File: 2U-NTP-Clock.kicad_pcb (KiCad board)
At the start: 2 copper layers, 482.6 x 83.8 mm, 279 parts, among them J1 Barrel_Jack_Switch, J2 Conn_01x06_Socket, Q1 BSS138, Q10 BSS138, Q11 BSS138, Q12 BSS138, Q13 BSS138, Q14 BSS138, Q15 BSS138, Q16 BSS138, Q17 BSS138, Q18 BSS138, Q19 BSS138, Q2 BSS138, Q20 BSS138, Q21 BSS138, Q22 BSS138, Q23 BSS138, Q24 BSS138, Q25 BSS138, Q26 BSS138, Q27 BSS138, Q28 BSS138, Q29 BSS138, Q3 BSS138, Q30 BSS138, Q31 BSS138, Q32 BSS138, Q33 BSS138, Q34 BSS138, Q35 BSS138, Q36 BSS138, Q37 BSS138, Q38 BSS138, Q39 BSS138, Q4 BSS138, Q40 BSS138, Q41 BSS138, Q42 BSS138, Q43 BSS138, Q5 BSS138, Q6 BSS138, Q7 BSS138, Q8 BSS138, Q9 BSS138, SW1 SW_Push, SW2 SW_Push, SW3 SW_Push, SW4 SW_Push, SW5 SW_Push, SW6 SW_Slide_DPDT, U3 74HC595, U4 74HC595, U5 74HC595, U6 74HC595, U7 74HC595, U8 74HC595, U9 L7805

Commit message: 基板概形修正
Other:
- board size 482.6 x 83.8 mm -> 482.6 x 87.8 mm
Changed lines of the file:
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@@
 	)
 	(gr_arc
-		(start 546.099999 241.299998)
-		(mid 544.984076 243.994075)
-		(end 542.289999 245.109998)
+		(start 546.1 243.332)
+		(mid 544.984077 246.026078)
+		(end 542.29 247.142)
 		(stroke
 			(width 0.05)
@@
 	)
 	(gr_line
-		(start 67.31 161.289999)
-		(end 542.289999 161.29)
+		(start 114.935 166.116)
+		(end 114.935 173.609)
 		(stroke
 			(width 0.05)
@@
 	)
 	(gr_arc
-		(start 539.242 174.243999)
-		(mid 542.798 177.799999)
-		(end 539.242 181.355999)
+		(start 118.745 173.609)
+		(mid 118.521815 174.147815)
+		(end 117.983 174.371)
 		(stroke
 			(width 0.05)
@@
 	)
 	(gr_line
-		(start 73.66 232.155999)
-		(end 70.358 232.155999)
+		(start 67.310001 159.384999)
+		(end 542.29 159.385)
 		(stroke
 			(width 0.05)
@@
 	)
 	(gr_arc
-		(start 535.94 232.155999)
-		(mid 532.384 228.599999)
-		(end 535.94 225.043999)
+		(start 539.242 177.418999)
+		(mid 542.798001 180.975)
+		(end 539.242 184.530999)
 		(stroke
 			(width 0.05)
@@
 	)
 	(gr_line
-		(start 63.5 241.299999)
-		(end 63.5 165.099999)
+		(start 73.66 228.980999)
+		(end 70.358 228.980999)
 		(stroke
 			(width 0.05)
@@
 	)
 	(gr_arc
-		(start 73.66 225.043999)
-		(mid 77.216 228.599999)
-		(end 73.66 232.155999)
+		(start 535.94 228.980999)
+		(mid 532.384001 225.425)
+		(end 535.94 221.868999)
+		(stroke
+			(width 0.05)
+			(type default)
+		)
+		(layer "Edge.Cuts")
+	)
+	(gr_line
+		(start 63.500001 243.332001)
+		(end 63.500001 163.194999)
+		(stroke
+			(width 0.05)
+			(type default)
+		)
+		(layer "Edge.Cuts")
+	)
+	(gr_arc
+		(start 73.66 221.868999)
+		(mid 77.216001 225.425)
+		(end 73.66 228.980999)
+		(stroke
+			(width 0.05)
+			(type default)
+		)
+		(layer "Edge.Cuts")
+	)
+	(gr_arc
+		(start 539.242 221.868999)
+		(mid 542.798001 225.425)
+		(end 539.242 228.980999)
+		(stroke
+			(width 0.05)
+			(type default)
+		)
+		(layer "Edge.Cuts")
+	)
+	(gr_line
+		(start 539.242 228.980999)
+		(end 535.94 228.980999)
 		(stroke
 			(width 0.05)
@@
 	)
 	(gr_arc
-		(start 539.242 225.043999)
-		(mid 542.798 228.599999)
-		(end 539.242 232.155999)
+		(start 535.94 184.530999)
+		(mid 532.384001 180.975)
+		(end 535.94 177.418999)
 		(stroke
 			(width 0.05)
@@
 	)
 	(gr_line
-		(start 539.242 232.155999)
-		(end 535.94 232.155999)
+		(start 118.745 173.609)
+		(end 118.745 166.116)
 		(stroke
 			(width 0.05)
@@
 	)
 	(gr_arc
-		(start 535.94 181.355999)
-		(mid 532.384 177.799999)
-		(end 535.94 174.243999)
+		(start 67.310001 247.142001)
+		(mid 64.615925 246.026078)
+		(end 63.500001 243.332001)
+		(stroke
+			(width 0.05)
+			(type default)
+		)
+		(layer "Edge.Cuts")
+	)
+	(gr_line
+		(start 542.29 247.142)
+		(end 67.310001 247.142001)
 		(stroke
 			(width 0.05)
@@
 	)
 	(gr_arc
-		(start 67.31 245.109999)
-		(mid 64.615923 243.994076)
-		(end 63.5 241.299999)
+		(start 70.358 228.980999)
+		(mid 66.802001 225.425)
+		(end 70.358 221.868999)
 		(stroke
 			(width 0.05)
@@
 	)
 	(gr_line
-		(start 542.289999 245.109998)
-		(end 67.31 245.109999)
+		(start 546.1 163.322)
+		(end 546.1 243.332)
 		(stroke
 			(width 0.05)
@@
 	)
 	(gr_arc
-		(start 70.358 232.155999)
-		(mid 66.802 228.599999)
-		(end 70.358 225.043999)
+		(start 115.697 174.371)
+		(mid 115.158185 174.147815)
+		(end 114.935 173.609)
+		(stroke
+			(width 0.05)
+			(type default)
+		)
+		(layer "Edge.Cuts")
+	)
+	(gr_line
+		(start 115.697 174.371)
+		(end 117.983 174.371)
 		(stroke
 			(width 0.05)
@@
 	)
 	(gr_line
-		(start 546.099999 165.1)
-		(end 546.1 241.299999)
+		(start 539.242 184.530999)
+		(end 535.94 184.530999)
 		(stroke
 			(width 0.05)
@@
 	)
 	(gr_line
-		(start 539.242 181.355999)
-		(end 535.94 181.355999)
+		(start 73.66 184.530999)
+		(end 70.358 184.530999)
 		(stroke
 			(width 0.05)
@@
 	)
 	(gr_line
-		(start 73.66 181.355999)
-		(end 70.358 181.355999)
+		(start 115.697 165.354)
+		(end 117.983 165.354)
 		(stroke
 			(width 0.05)
@@
 	)
 	(gr_line
-		(start 70.358 225.043999)
-		(end 73.66 225.043999)
+		(start 70.358 221.868999)
+		(end 73.66 221.868999)
+		(stroke
+			(width 0.05)
+			(type default)
+		)
+		(layer "Edge.Cuts")
+	)
+	(gr_arc
+		(start 63.500001 163.194999)
+		(mid 64.615925 160.500923)
+		(end 67.310001 159.384999)
+		(stroke
+			(width 0.05)
+			(type default)
+		)
+		(layer "Edge.Cuts")
+	)
+	(gr_arc
+		(start 117.983 165.354)
+		(mid 118.521815 165.577185)
+		(end 118.745 166.116)
 		(stroke
 			(width 0.05)
@@
 	)
 	(gr_arc
-		(start 63.5 165.099999)
-		(mid 64.615923 162.405922)
-		(end 67.31 161.289999)
+		(start 542.29 159.385)
+		(mid 544.984077 160.500923)
+		(end 546.1 163.195)
 		(stroke
 			(width 0.05)
@@
 	)
 	(gr_arc
-		(start 542.289999 161.29)
-		(mid 544.984076 162.405923)
-		(end 546.099999 165.1)
+		(start 114.935 166.116)
+		(mid 115.158185 165.577185)
+		(end 115.697 165.354)
 		(stroke
 			(width 0.05)
@@
 	)
 	(gr_arc
-		(start 73.66 174.243999)
-		(mid 77.216 177.799999)
-		(end 73.66 181.355999)
+		(start 73.66 177.418999)
+		(mid 77.216001 180.975)
+		(end 73.66 184.530999)
 		(stroke
 			(width 0.05)
@@
 	)
 	(gr_line
-		(start 535.94 225.043999)
-		(end 539.242 225.043999)
+		(start 535.94 221.868999)
+		(end 539.242 221.868999)
 		(stroke
 			(width 0.05)
@@
 	)
 	(gr_line
-		(start 70.358 174.243999)
-		(end 73.66 174.243999)
+		(start 70.358 177.418999)
+		(end 73.66 177.418999)
 		(stroke
 			(width 0.05)
@@
 	)
 	(gr_arc
-		(start 70.358 181.355999)
-		(mid 66.802 177.799999)
-		(end 70.358 174.243999)
+		(start 70.358 184.530999)
+		(mid 66.802001 180.975)
+		(end 70.358 177.418999)
 		(stroke
 			(width 0.05)
@@
 	)
 	(gr_line
-		(start 535.94 174.243999)
-		(end 539.242 174.243999)
+		(start 535.94 177.418999)
+		(end 539.242 177.418999)
 		(stroke
 			(width 0.05)
@@
 		(polygon
 			(pts
-				(xy 79.756 161.29) (xy 79.756 245.11) (xy 529.844 245.11) (xy 529.844 161.29)
+				(xy 82.042 159.385) (xy 82.042 247.142) (xy 527.558 247.142) (xy 527.558 159.385)
 			)
 		)
@@
 		(polygon
 			(pts
-				(xy 79.756 161.29) (xy 79.756 245.11) (xy 529.844 245.11) (xy 529.844 161.29)
+				(xy 82.042 159.385) (xy 82.042 247.142) (xy 527.558 247.142) (xy 527.558 159.385)
 			)
 		)

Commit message: シルクのバージョンアップ
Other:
- board text added: "2U NTP Clock Ver-0.2 MOS@53175DDD"
- board text removed: "2U NTP Clock Ver-0.1 MOS@53175DDD"
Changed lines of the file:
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@@
 		)
 	)
-	(gr_text "2U NTP Clock Ver-0.1\nMOS@53175DDD"
+	(gr_text "2U NTP Clock Ver-0.2\nMOS@53175DDD"
 		(at 474.98 238.506 0)
 		(layer "F.SilkS")

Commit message: コンフリクト修正
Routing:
- net /OK: track 464.5 -> 437.9 mm
- net /RIGHT: track 478.0 -> 464.7 mm
- net /UP: track 450.1 -> 437.6 mm
- net /DOWN: track 431.8 -> 424.8 mm
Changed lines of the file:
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@@
-	)
-	(segment
-		(start 479.806 184.658)
-		(end 496.098 200.95)
-		(width 0.2)
-		(layer "B.Cu")
-		(net 3)
 	)
 	(segment
@@
 		(start 104.902 221.234)
 		(end 104.902 218.636314)
-		(width 0.2)
-		(layer "B.Cu")
-		(net 3)
-	)
-	(segment
-		(start 496.098 200.95)
-		(end 499.67 200.95)
 		(width 0.2)
 		(layer "B.Cu")
@@
 	)
 	(segment
-		(start 487.208 190.79)
-		(end 499.67 190.79)
-		(width 0.2)
-		(layer "B.Cu")
-		(net 5)
-	)
-	(segment
 		(start 468.884 182.626)
 		(end 419.1 182.626)
@@
 	)
 	(segment
-		(start 471.17 183.642)
-		(end 479.355686 183.642)
-		(width 0.2)
-		(layer "B.Cu")
-		(net 14)
-	)
-	(segment
 		(start 247.904 180.594)
 		(end 242.316 180.594)
@@
 	)
 	(segment
-		(start 506.17 198.628)
-		(end 508.492 200.95)
-		(width 0.2)
-		(layer "B.Cu")
-		(net 14)
-	)
-	(segment
 		(start 416.814 183.642)
 		(end 370.332 183.642)
@@
 	)
 	(segment
-		(start 508.492 200.95)
-		(end 510.286 200.95)
-		(width 0.2)
-		(layer "B.Cu")
-		(net 14)
-	)
-	(segment
 		(start 136.652 183.642)
 		(end 130.302 189.992)
@@
 		(width 0.2)
 		(layer "B.Cu")
-		(net 17)
-	)
-	(segment
-		(start 470.662 192.278)
-		(end 477.732314 192.278)
-		(width 0.2)
-		(layer "B.Cu")

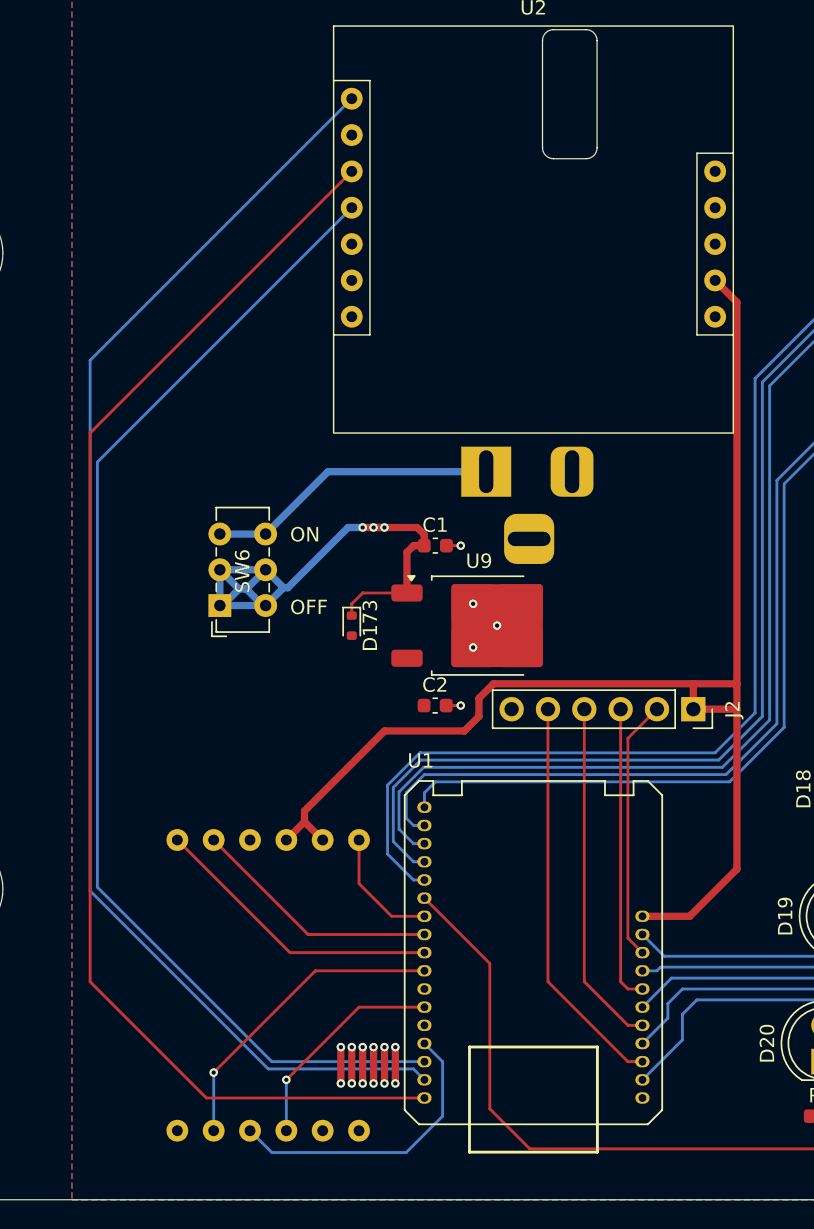
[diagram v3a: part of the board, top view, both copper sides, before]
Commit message: アップデート
ランドの径の変更
配線取り回しの変更
など
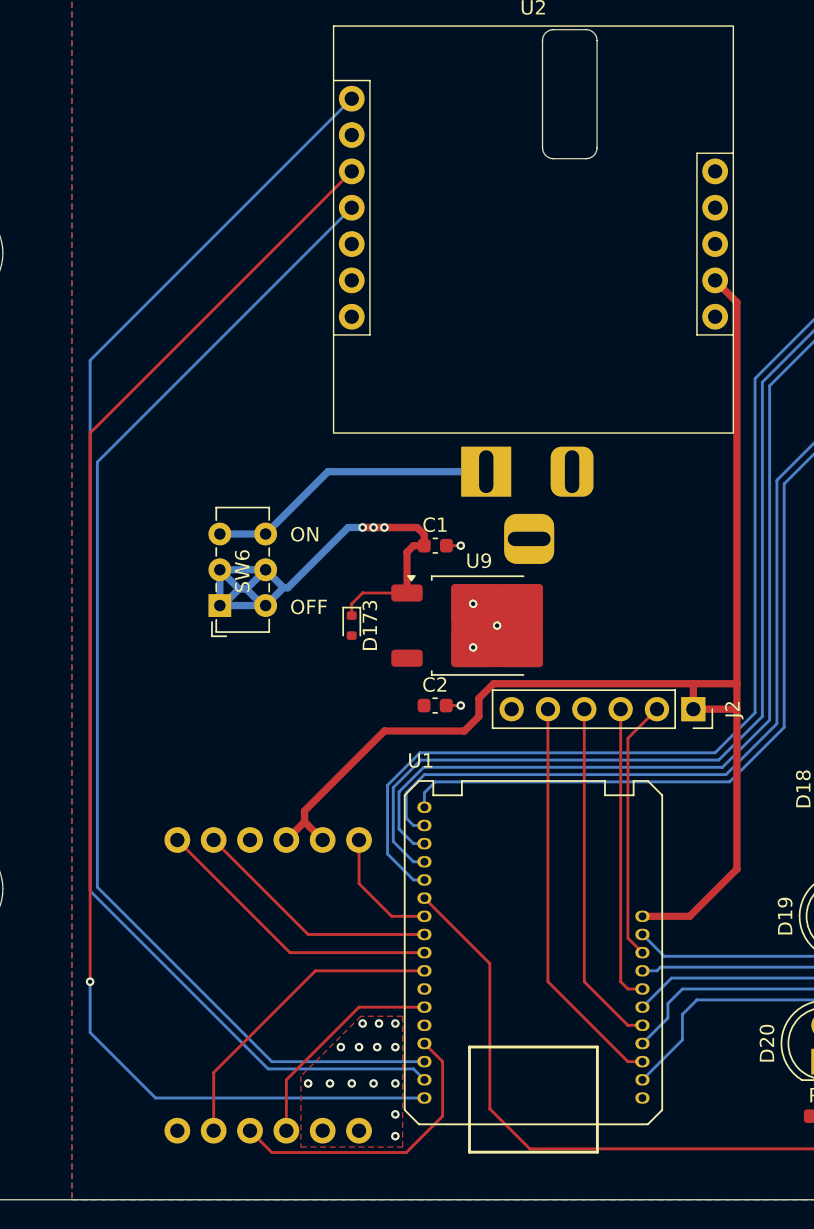
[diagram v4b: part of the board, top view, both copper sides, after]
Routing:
- net GND: track 78.3 -> 63.1 mm, vias 66 -> 68
- net SCL: track 91.0 -> 93.0 mm, vias 0 -> 1
- net /MOSI: vias 1 -> 0
- net /CS: vias 1 -> 0
- added copper zone on F.Cu, net GND
